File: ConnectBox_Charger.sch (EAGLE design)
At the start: 1 part, among them J1 CONNECTOR_PI_40_PIN

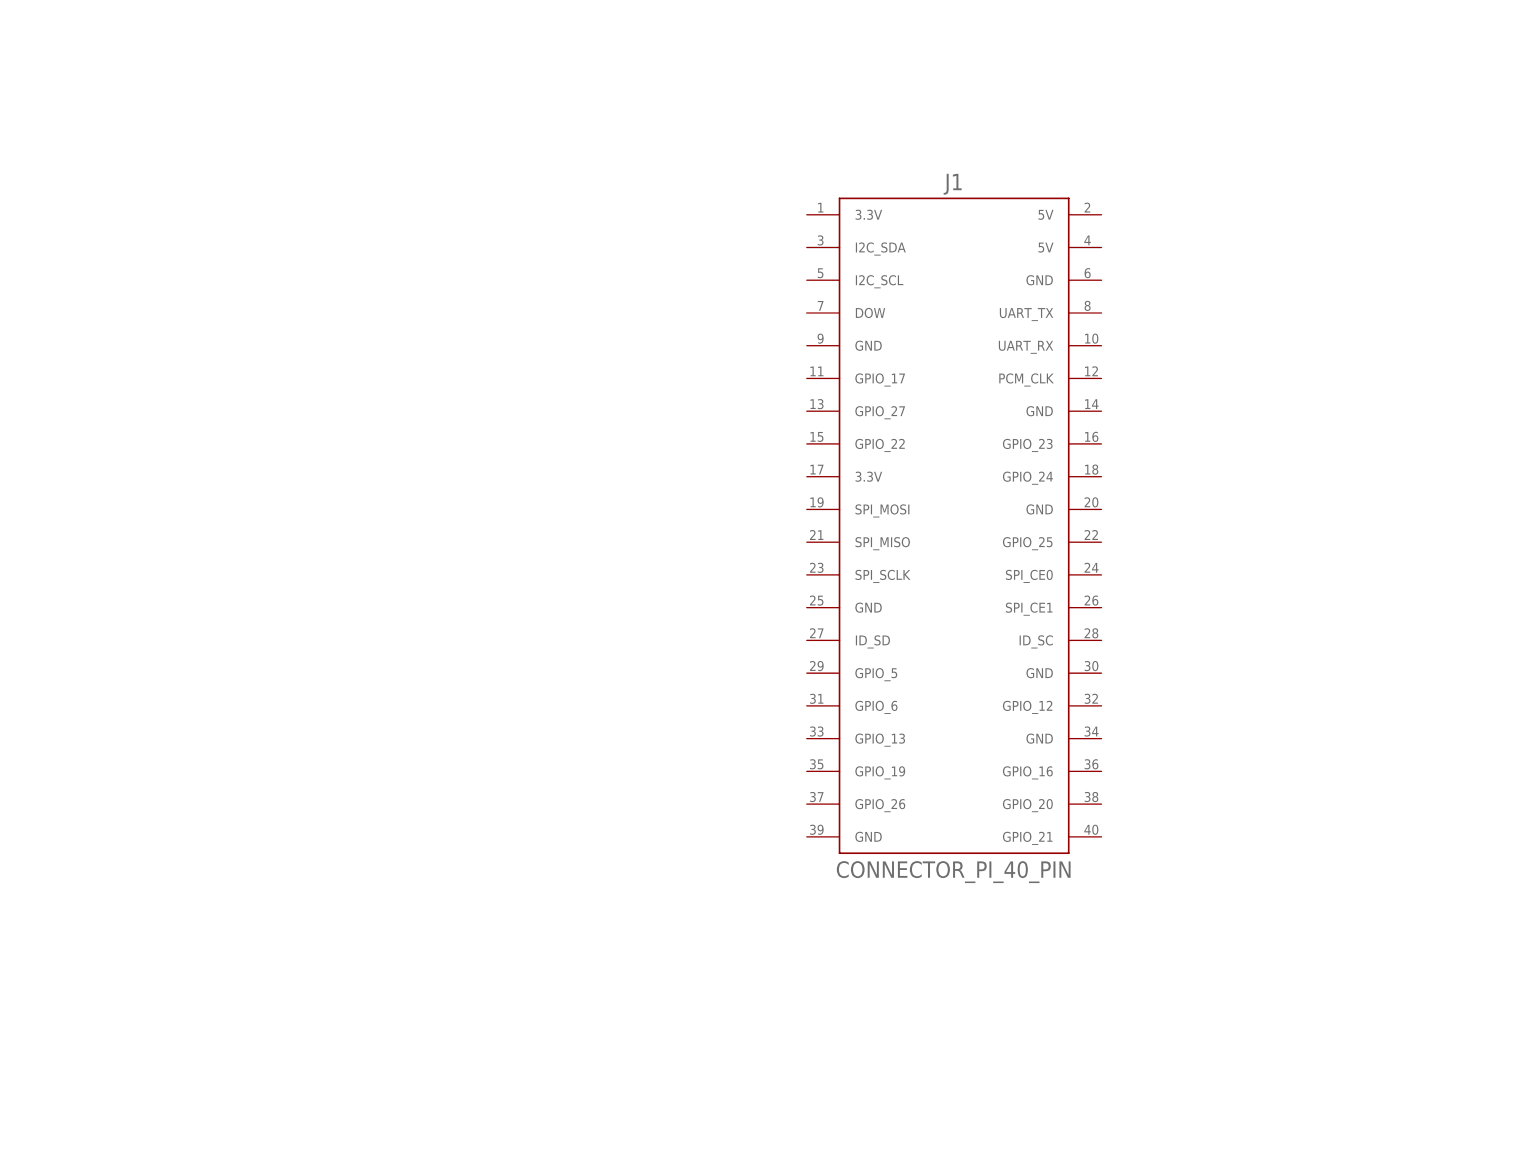
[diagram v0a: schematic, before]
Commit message: Add LTC4040 Breakout
Breakout from an Analog Devices/Linear Technology LTC4040 “2.5A Battery Backup Power Manager” IC. Boost SMPS with 5V out, and buck SMPS to charge lithium cell. Li-Ion selectable 3.95V/4.0V/4.05V/4.1V Lithium Iron Phosphate LiFePO4 selectable 3.45V/3.5V/3.55V/3.6V

https://www.analog.com/en/products/ltc4040.html
https://www.analog.com/media/en/technical-documentation/data-sheets/4040fb.pdf

Package UFD, QFN 4mm x 5mm. 24 pins plus Exposed Pad. LTC4040EUFD
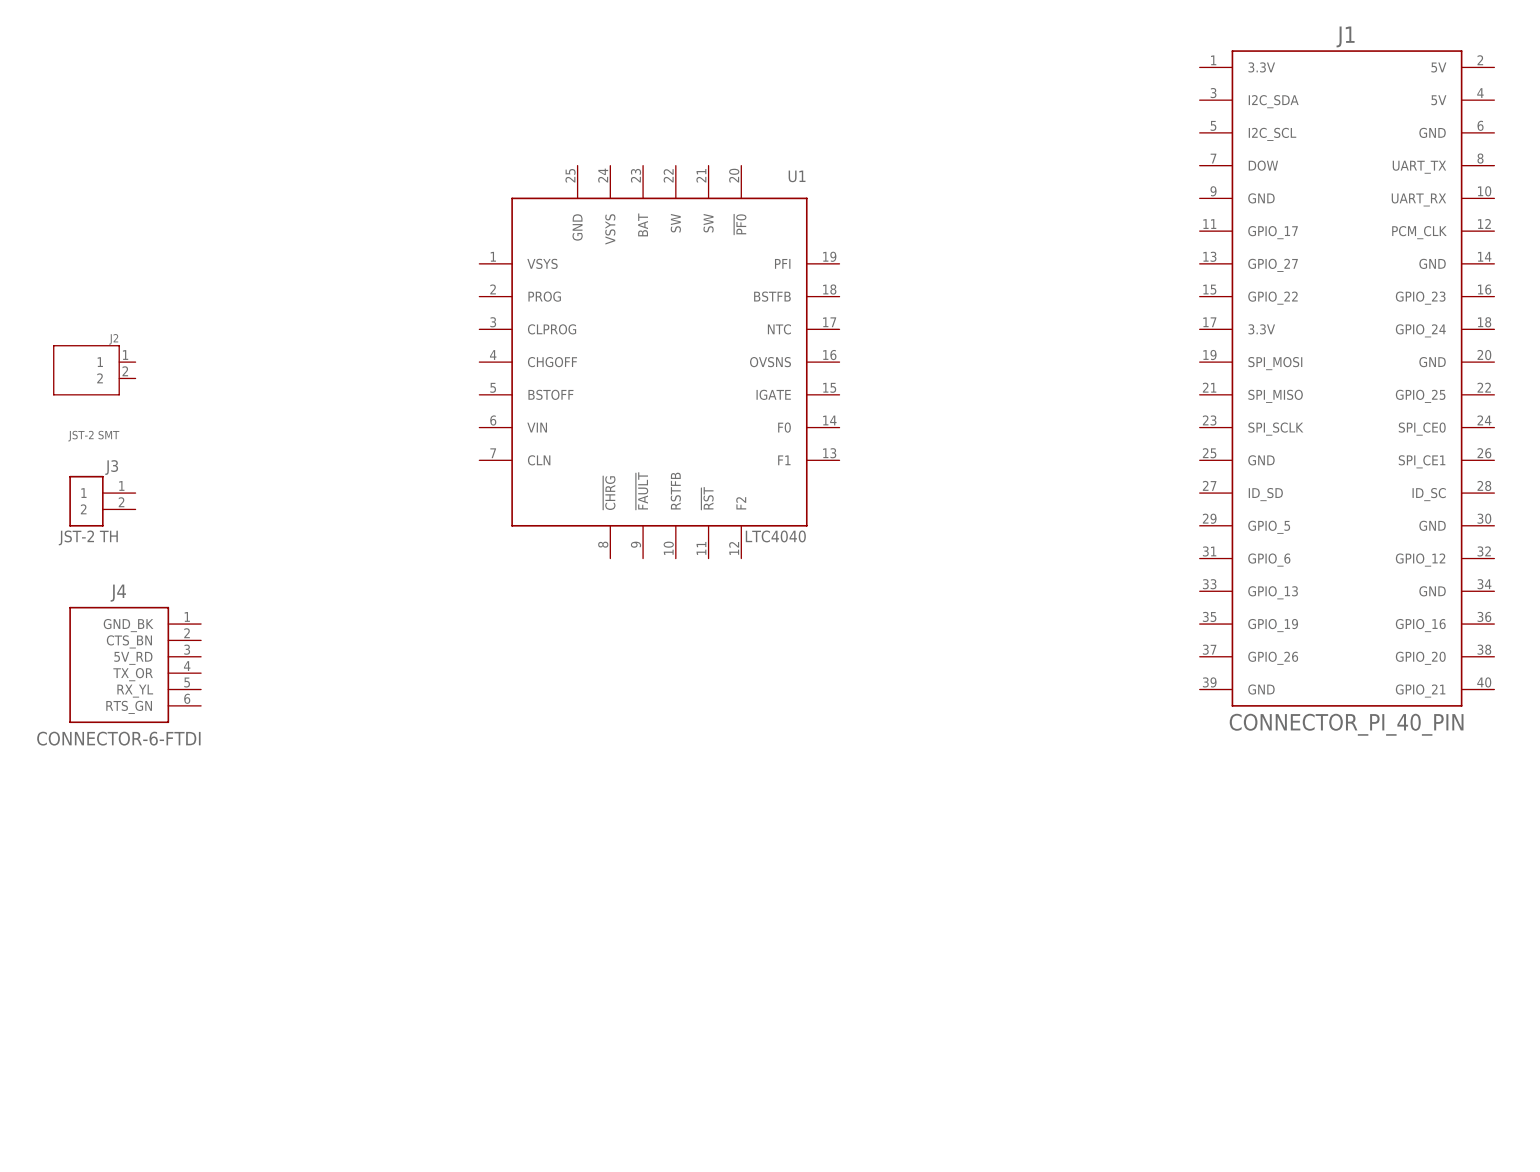
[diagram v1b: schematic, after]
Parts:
- added J2: JST-2 SMT, ConnectBox_2019:S2B-PH-SM4-TB(LF)(SN)
- added J3: JST-2 TH, ConnectBox_2019:S2B-PH-K-S(LF)(SN)
- added J4: CONNECTOR-6-FTDI, ConnectBox_2019:CONNECTOR-6-FTDI
- added U1: LTC4040, ConnectBox_2019:LTC4040
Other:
- note added: "Todo: Inductor HAT EEPROM USB A Female"
- moved on the sheet: J1
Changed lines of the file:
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@@
 <setting verticaltext="up"/>
 </settings>
-<grid distance="0.1" unitdist="inch" unit="inch" style="lines" multiple="1" display="no" altdistance="0.01" altunitdist="inch" altunit="inch"/>
+<grid distance="0.1" unitdist="inch" unit="inch" style="lines" multiple="1" display="yes" altdistance="0.01" altunitdist="inch" altunit="inch"/>
 <layers>
 <layer number="1" name="Top" color="4" fill="1" visible="no" active="no"/>
@@
 <part name="FRAME1" library="ConnectBox_2019" deviceset="FRAMES_LETTER_L" device=""/>
 <part name="J1" library="ConnectBox_2019" deviceset="CONNECTOR_PI_40_PIN" device=""/>
+<part name="J2" library="ConnectBox_2019" deviceset="S2B-PH-SM4-TB(LF)(SN)" device="" value="JST-2 SMT"/>
+<part name="J3" library="ConnectBox_2019" deviceset="S2B-PH-K-S(LF)(SN)" device="" value="JST-2 TH"/>
+<part name="U1" library="ConnectBox_2019" deviceset="LTC4040" device=""/>
+<part name="J4" library="ConnectBox_2019" deviceset="CONNECTOR-6-FTDI" device=""/>
 </parts>
 <sheets>
 <sheet>
 <plain>
+<text x="-2.54" y="185.42" size="3.81" layer="89" align="top-right">  Todo:
+Inductor
+HAT EEPROM
+USB A Female</text>
 </plain>
 <instances>
@@
 <attribute name="DRAWING_NAME" x="165.1" y="19.05" size="2.54" layer="94"/>
 </instance>
-<instance part="J1" gate="G$1" x="147.32" y="101.6" smashed="yes">
-<attribute name="NAME" x="147.32" y="154.94" size="2.54" layer="95" align="center"/>
-<attribute name="VALUE" x="147.32" y="48.26" size="2.54" layer="96" align="center"/>
+<instance part="J1" gate="G$1" x="208.28" y="124.46" smashed="yes">
+<attribute name="NAME" x="208.28" y="177.8" size="2.54" layer="95" align="center"/>
+<attribute name="VALUE" x="208.28" y="71.12" size="2.54" layer="96" align="center"/>
+</instance>
+<instance part="J2" gate="G$1" x="12.7" y="124.46" smashed="yes" rot="MR0">
+<attribute name="NAME" x="17.7829" y="130.05571875" size="1.272509375" layer="95" rot="MR0"/>
+<attribute name="VALUE" x="17.78811875" y="115.03731875" size="1.275409375" layer="96" rot="MR0"/>
+</instance>
+<instance part="J3" gate="G$1" x="12.7" y="106.68" smashed="yes" rot="MR0">
+<attribute name="NAME" x="17.78" y="109.982" size="1.778" layer="95" rot="MR0"/>
+<attribute name="VALUE" x="17.78" y="99.06" size="1.778" layer="96" rot="MR0"/>
+</instance>
+<instance part="U1" gate="G$1" x="101.6" y="127" smashed="yes">
+<attribute name="NAME" x="124.46" y="154.94" size="1.778" layer="95" align="bottom-right"/>
+<attribute name="VALUE" x="124.46" y="99.06" size="1.778" layer="96" align="bottom-right"/>
+</instance>
+<instance part="J4" gate="G$1" x="17.78" y="81.28" smashed="yes">
+<attribute name="VALUE" x="17.78" y="68.58" size="2.0828" layer="96" rot="R180" align="center"/>
+<attribute name="NAME" x="17.78" y="91.44" size="2.0828" layer="95" rot="R180" align="center"/>
 </instance>
 </instances>
@@
 </drawing>
 <compatibility>
+<note version="6.3" minversion="6.2.2" severity="warning">
+Since Version 6.2.2 text objects can contain more than one line,
+which will not be processed correctly with this version.
+</note>
 <note version="8.3" severity="warning">
 Since Version 8.3, EAGLE supports URNs for individual library

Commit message: Continue Charger Schematic and Library Parts Add USB A Receptacle, microUSB Power in, decide on SMT for JST-2, start to add nets.
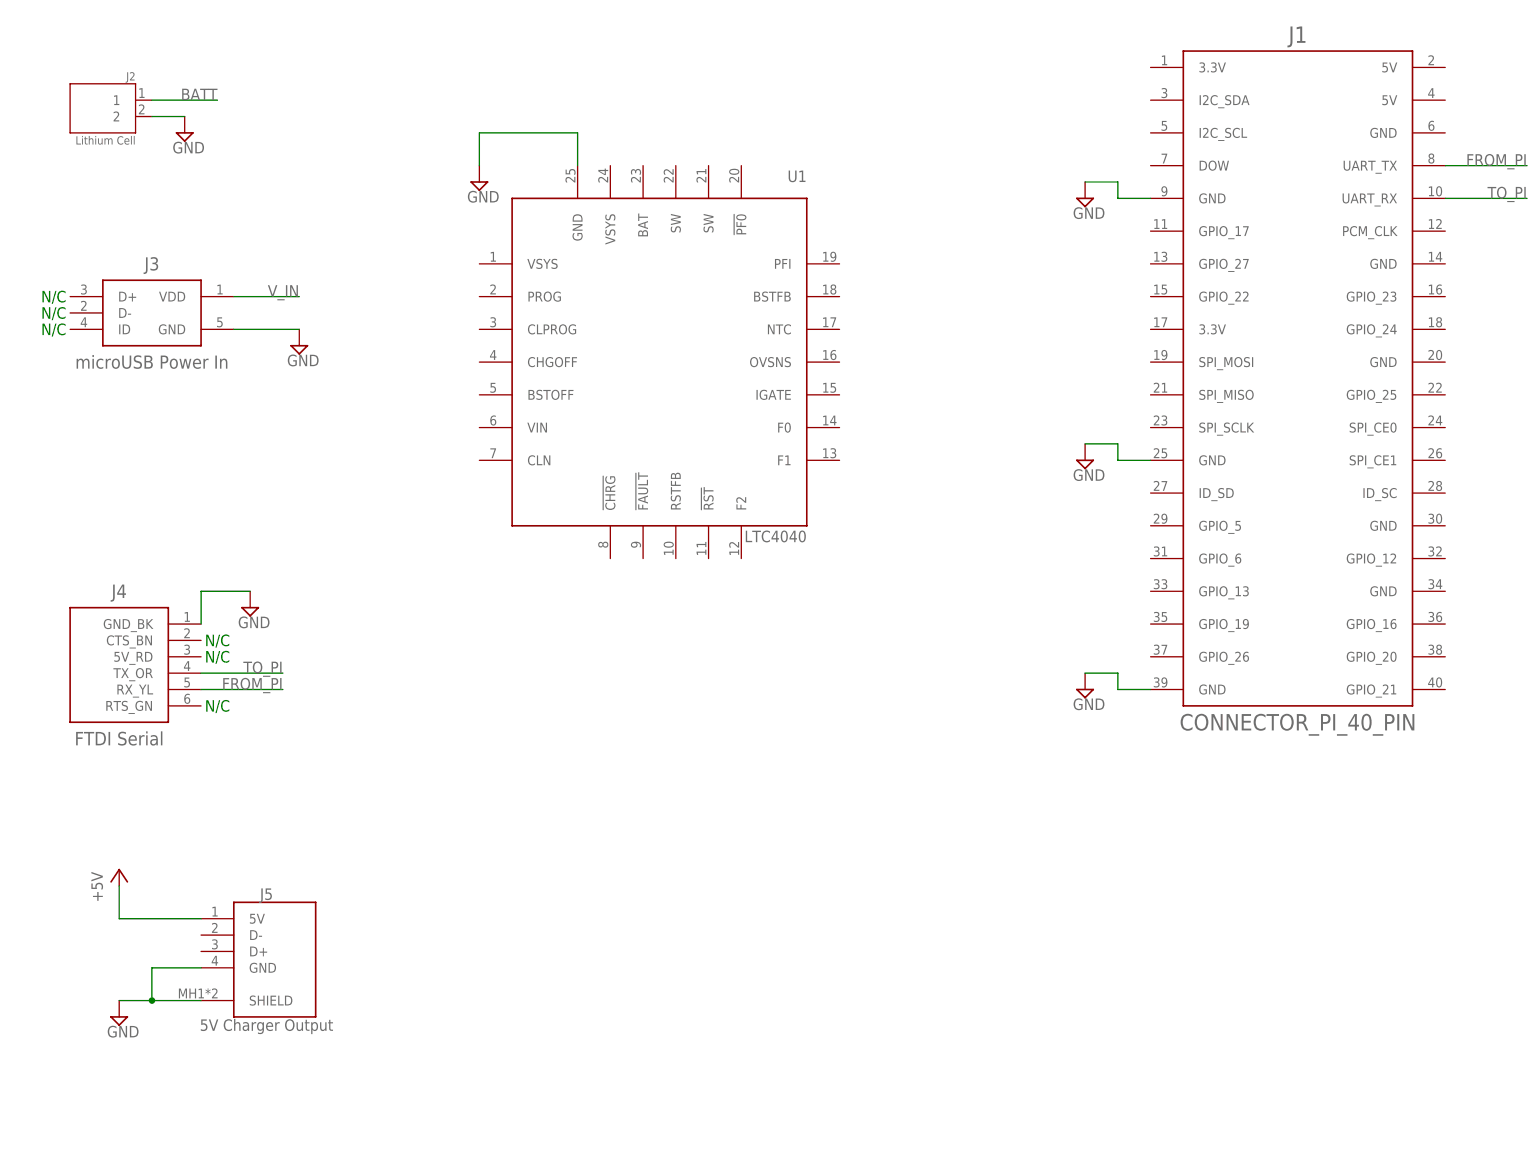
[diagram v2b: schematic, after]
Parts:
- added J5: 5V Charger Output, ConnectBox_2019:SS-52100-001
- J2: value JST-2 SMT -> Lithium Cell
- J3: value JST-2 TH -> microUSB Power In; device ConnectBox_2019:S2B-PH-K-S(LF)(SN) -> ConnectBox_2019:10118194-0001LF
- J4: value CONNECTOR-6-FTDI -> FTDI Serial
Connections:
- new net +5V: J5.5V@1
- new net BATT: J2.1
- new net FROM_PI: J1.UART_TX@8, J4.RX_YL@5
- new net GND: J1.GND@25, J1.GND@39, J1.GND@9, J2.2, J3.GND, J4.GND_BK@1, J5.GND@4, J5.SHIELD, U1.GND@25
- new net TO_PI: J1.UART_RX@10, J4.TX_OR@4
- new net V_IN: J3.VDD
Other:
- note added: "N/C"
- note added: "Todo: Inductor HAT EEPROM Resistors at USB-A to indicate output current"
- note removed: "Todo: Inductor HAT EEPROM USB A Female"
- moved on the sheet: J1, J2

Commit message: Add parts to library, Schematic. Add LTC4040 IC, inductor, 4x DIP switch, table of settings for Battery Chemistry, charging Voltage.
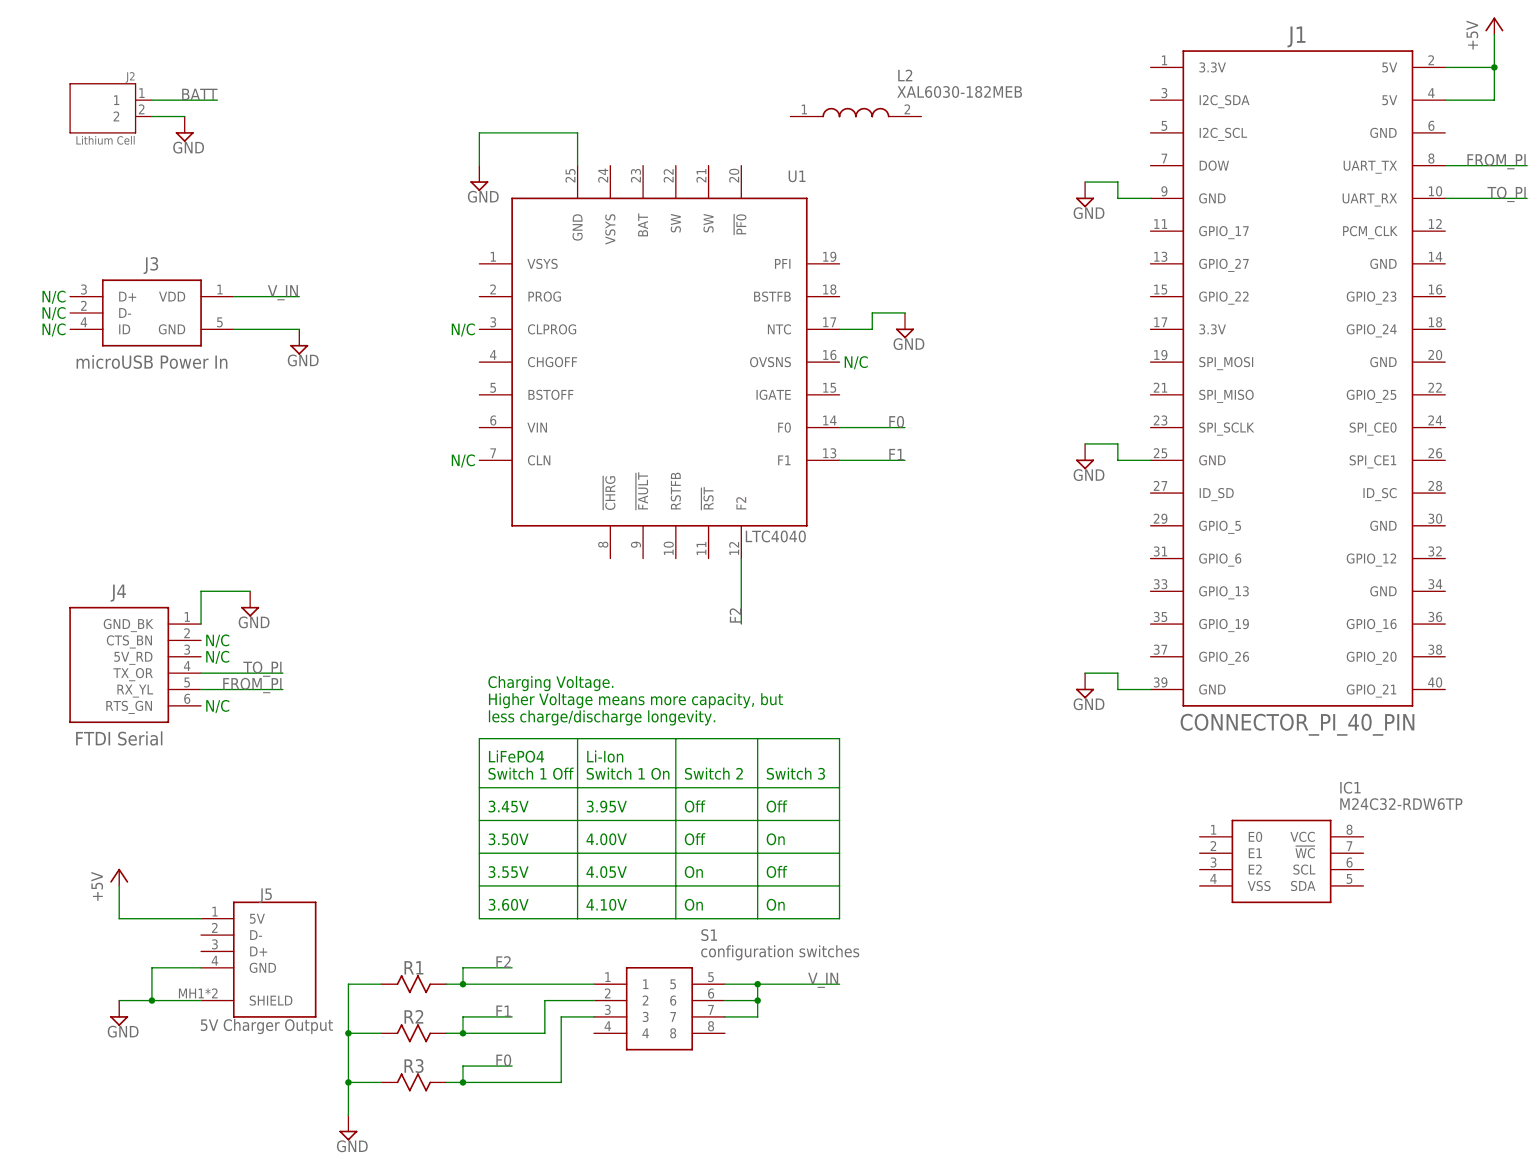
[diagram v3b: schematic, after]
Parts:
- added IC1: M24C32-RDW6TP, ConnectBox_2019:M24C32-RDW6TP
- added L2: XAL6030-182MEB, ConnectBox_2019:XAL6030-182MEB
- added R1, R2, R3: (no value), ConnectBox_2019:RESISTOR0603
- added S1: configuration switches, ConnectBox_2019:219-4LPST
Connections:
- new net F0: R3.2, S1.3, U1.F0@14
- new net F1: R2.2, S1.2, U1.F1@13
- new net F2: R1.2, S1.1, U1.F2@12
- net +5V: now also J1.5V@2, J1.5V@4
- net GND: now also R1.1, R2.1, R3.1, U1.NTC@17
- net V_IN: now also S1.5, S1.6, S1.7
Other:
- note added: "3.45V"
- note added: "3.50V"
- note added: "3.55V"
- note added: "3.60V"
- note added: "3.95V"
- note added: "4.00V"
- note added: "4.05V"
- note added: "4.10V"
- note added: "Charging Voltage. Higher Voltage means more capacity, but less charge/discharge longevity."
- note added: "Li-Ion Switch 1 On"
- note added: "LiFePO4 Switch 1 Off"
- note added: "Off"
- note added: "On"
- note added: "Switch 2"
- note added: "Switch 3"
- note added: "Todo: Resistors at USB-A to indicate output current"
- note removed: "Todo: Inductor HAT EEPROM Resistors at USB-A to indicate output current"
